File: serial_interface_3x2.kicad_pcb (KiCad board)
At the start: 2 copper layers, 70.5 x 41.9 mm, 9 parts, among them J1 DB9M_RA, U1 RS232_2x2

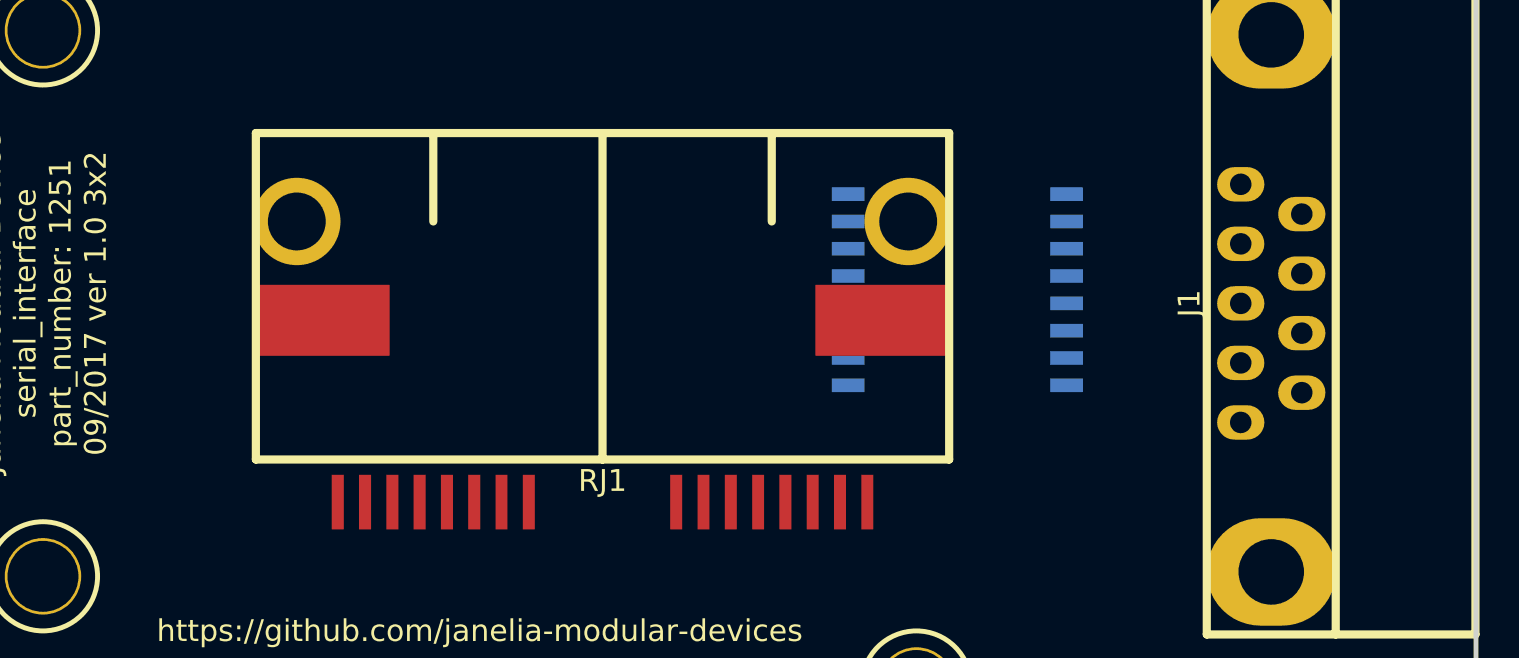
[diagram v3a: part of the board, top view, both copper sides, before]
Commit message: Added text to footprint.
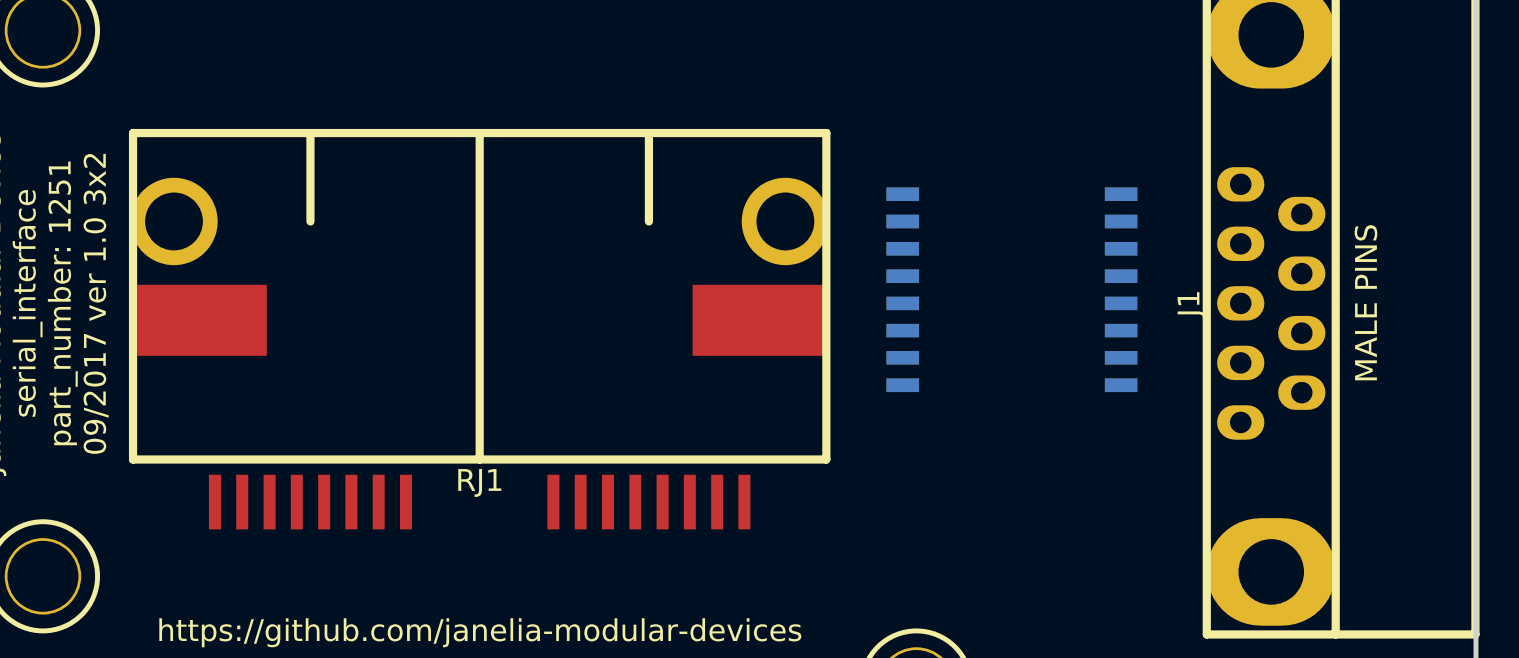
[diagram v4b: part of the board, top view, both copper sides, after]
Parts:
- moved RJ1 5.71 mm to (109.9, 85.1)
- moved U1 2.54 mm to (134.6, 88.9)
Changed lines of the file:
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@@
     (diff_pair_width 0.254)
   )
+  (module serial_interface_3x2:DB9M_RA (layer F.Cu)
+    (at 146.685 88.9 90)
+    (fp_text reference J1 (at 0 -3.81 90) (layer F.SilkS)
+      (effects (font (size 1.016 1.016) (thickness 0.254)))
+    )
+    (fp_text value DB9M_RA (at 0 4.445 90) (layer F.Fab)
+      (effects (font (size 1.016 1.016) (thickness 0.254)))
+    )
+    (fp_text user "MALE PINS" (at 0 4.445 90) (layer F.SilkS)
+      (effects (font (size 1.016 1.016) (thickness 0.254)))
+    )
+    (fp_line (start -8.46 9.5) (end -8.46 15.6) (layer F.Fab) (width 0.381))
+    (fp_line (start -8.46 15.6) (end 8.46 15.6) (layer F.Fab) (width 0.381))
+    (fp_line (start 8.46 15.6) (end 8.46 9.5) (layer F.Fab) (width 0.381))
+    (fp_line (start -15.405 9.5) (end 15.405 9.5) (layer F.SilkS) (width 0.381))
+    (fp_line (start 15.405 -3) (end 15.405 9.5) (layer F.SilkS) (width 0.381))
+    (fp_line (start -15.405 3) (end 15.405 3) (layer F.SilkS) (width 0.381))
+    (fp_line (start -15.405 -3) (end -15.405 9.5) (layer F.SilkS) (width 0.381))
+    (fp_line (start -15.405 -3) (end 15.405 -3) (layer F.SilkS) (width 0.381))
+    (pad "" thru_hole oval (at -12.495 0 90) (size 5 6) (drill 3.05) (layers *.Cu *.Mask))
+    (pad "" thru_hole oval (at 12.492 0 90) (size 5 6) (drill 3.05) (layers *.Cu *.Mask))
+    (pad 1 thru_hole oval (at -5.54 -1.42 90) (size 1.6 2.2) (drill 1) (layers *.Cu *.Mask))
+    (pad 2 thru_hole oval (at -2.77 -1.42 90) (size 1.6 2.2) (drill 1) (layers *.Cu *.Mask)
+      (net 10 /RD))
+    (pad 3 thru_hole oval (at 0 -1.42 90) (size 1.6 2.2) (drill 1) (layers *.Cu *.Mask)
+      (net 9 /TD))
+    (pad 4 thru_hole oval (at 2.77 -1.42 90) (size 1.6 2.2) (drill 1) (layers *.Cu *.Mask))
+    (pad 5 thru_hole oval (at 5.54 -1.42 90) (size 1.6 2.2) (drill 1) (layers *.Cu *.Mask)
+      (net 6 GND))
+    (pad 6 thru_hole oval (at -4.155 1.42 90) (size 1.6 2.2) (drill 1) (layers *.Cu *.Mask))
+    (pad 7 thru_hole oval (at -1.385 1.42 90) (size 1.6 2.2) (drill 1) (layers *.Cu *.Mask))
+    (pad 8 thru_hole oval (at 1.385 1.42 90) (size 1.6 2.2) (drill 1) (layers *.Cu *.Mask))
+    (pad 9 thru_hole oval (at 4.155 1.42 90) (size 1.6 2.2) (drill 1) (layers *.Cu *.Mask))
+  )
   (module serial_interface_3x2:SOIC_16 (layer B.Cu)
-    (at 132.08 88.9)
+    (at 134.62 88.9)
     (solder_mask_margin 0.1016)
     (clearance 0.1016)
@@
     )
   )
-  (module serial_interface_3x2:DB9M_RA (layer F.Cu)
-    (at 146.685 88.9 90)
-    (fp_text reference J1 (at 0 -3.81 90) (layer F.SilkS)
-      (effects (font (size 1.016 1.016) (thickness 0.254)))
-    )
-    (fp_text value DB9M_RA (at 0 4.445 90) (layer F.Fab)
-      (effects (font (size 1.016 1.016) (thickness 0.254)))
-    )
-    (fp_line (start -15.405 -3) (end 15.405 -3) (layer F.SilkS) (width 0.381))
-    (fp_line (start -15.405 -3) (end -15.405 9.5) (layer F.SilkS) (width 0.381))
-    (fp_line (start -15.405 3) (end 15.405 3) (layer F.SilkS) (width 0.381))
-    (fp_line (start 15.405 -3) (end 15.405 9.5) (layer F.SilkS) (width 0.381))
-    (fp_line (start -15.405 9.5) (end 15.405 9.5) (layer F.SilkS) (width 0.381))
-    (fp_line (start 8.46 15.6) (end 8.46 9.5) (layer F.Fab) (width 0.381))
-    (fp_line (start -8.46 15.6) (end 8.46 15.6) (layer F.Fab) (width 0.381))
-    (fp_line (start -8.46 9.5) (end -8.46 15.6) (layer F.Fab) (width 0.381))
-    (pad 9 thru_hole oval (at 4.155 1.42 90) (size 1.6 2.2) (drill 1) (layers *.Cu *.Mask))
-    (pad 8 thru_hole oval (at 1.385 1.42 90) (size 1.6 2.2) (drill 1) (layers *.Cu *.Mask))
-    (pad 7 thru_hole oval (at -1.385 1.42 90) (size 1.6 2.2) (drill 1) (layers *.Cu *.Mask))
-    (pad 6 thru_hole oval (at -4.155 1.42 90) (size 1.6 2.2) (drill 1) (layers *.Cu *.Mask))
-    (pad 5 thru_hole oval (at 5.54 -1.42 90) (size 1.6 2.2) (drill 1) (layers *.Cu *.Mask)
-      (net 6 GND))
-    (pad 4 thru_hole oval (at 2.77 -1.42 90) (size 1.6 2.2) (drill 1) (layers *.Cu *.Mask))
-    (pad 3 thru_hole oval (at 0 -1.42 90) (size 1.6 2.2) (drill 1) (layers *.Cu *.Mask)
-      (net 9 /TD))
-    (pad 2 thru_hole oval (at -2.77 -1.42 90) (size 1.6 2.2) (drill 1) (layers *.Cu *.Mask)
-      (net 10 /RD))
-    (pad 1 thru_hole oval (at -5.54 -1.42 90) (size 1.6 2.2) (drill 1) (layers *.Cu *.Mask))
-    (pad "" thru_hole oval (at 12.492 0 90) (size 5 6) (drill 3.05) (layers *.Cu *.Mask))
-    (pad "" thru_hole oval (at -12.495 0 90) (size 5 6) (drill 3.05) (layers *.Cu *.Mask))
-  )
   (module serial_interface_3x2:RJ45_8P8C_2PORT_1ROW_RA_SMD (layer F.Cu)
-    (at 115.57 85.09 180)
+    (at 109.855 85.09 180)
     (fp_text reference RJ1 (at 0 -12.065 180) (layer F.SilkS)
       (effects (font (size 1.016 1.016) (thickness 0.254)))
